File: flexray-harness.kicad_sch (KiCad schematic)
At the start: 9 parts, among them J2 CAN, J3 POWER, J4 FR1, J5 FR2, K2 G6K-2

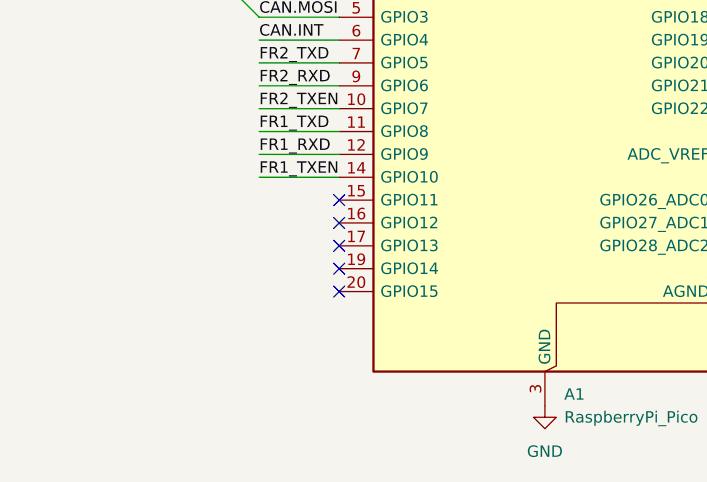
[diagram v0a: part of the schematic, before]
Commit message: connect relay pin to GPIO
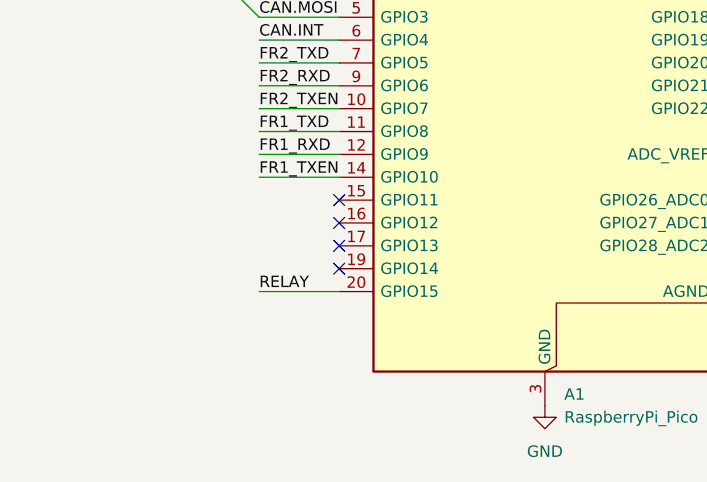
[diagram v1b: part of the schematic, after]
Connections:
- net RELAY: now also A1.20 (GPIO15)
- no-connect marks 21 -> 20
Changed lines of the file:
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@@
-	)
-	(no_connect
-		(at 62.23 157.48)
 	)
 	(no_connect
@@
 		(pts
 			(xy 53.34 121.92) (xy 62.23 121.92)
+		)
+		(stroke
+			(width 0)
+			(type default)
+		)
+	)
+	(wire
+		(pts
+			(xy 53.34 157.48) (xy 62.23 157.48)
 		)
 		(stroke
@@
 		(effects
 			(font
+				(size 1.27 1.27)
+			)
+			(justify left bottom)
+		)
+	)
+	(label "RELAY"
+		(at 53.34 157.48 0)
+		(effects
+			(font
